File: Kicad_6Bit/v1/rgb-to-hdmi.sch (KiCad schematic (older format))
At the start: 26 parts, among them P1 CONN_02X20, P2 Conn_02x05_Odd_Even, P3 Conn_01x06, P4 CONN_01X02, SW1 SW_PUSH, SW2 SW_PUSH, SW3 SW_PUSH, SW4 SW_PUSH, U1 XC9572XL-VQFP44

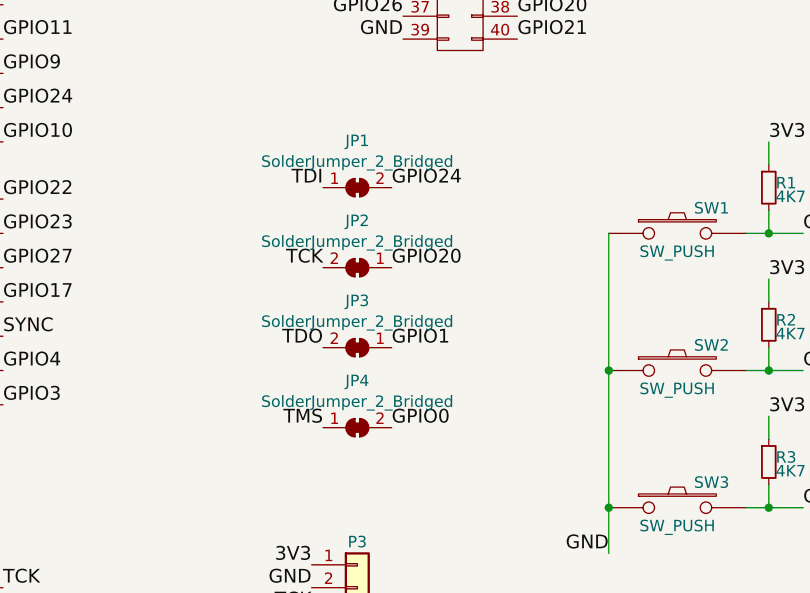
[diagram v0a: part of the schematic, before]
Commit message: Fix incorrect in system programming GPIO assignments
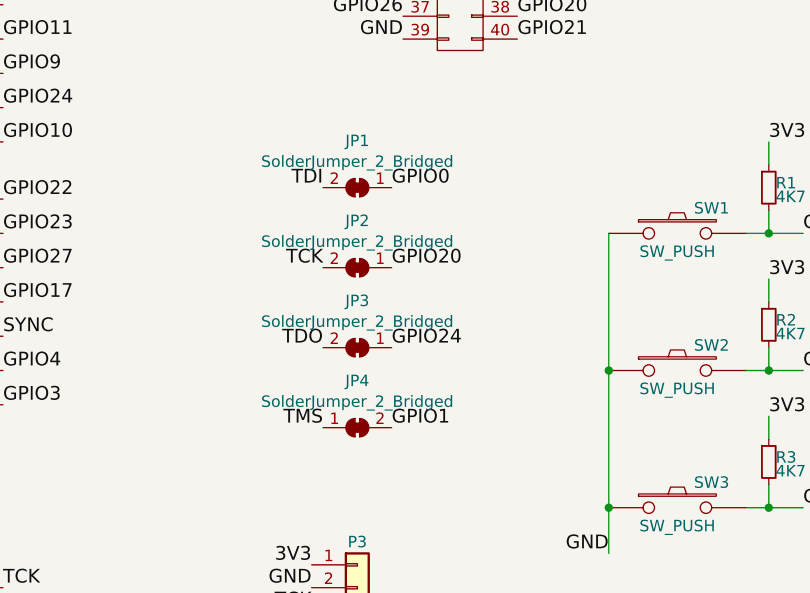
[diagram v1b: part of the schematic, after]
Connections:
- net GPIO0: now also JP1.1 (A); no longer JP4.2 (B)
- net GPIO1: now also JP4.2 (B); no longer JP3.1 (A)
- net GPIO24: now also JP3.1 (A); no longer JP1.2 (B)
- net TDI: now also JP1.2 (B); no longer JP1.1 (A)
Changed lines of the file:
@@
 TDO
 Text Label 8400 4750 0    60   ~ 0
-GPIO0
+GPIO1
 Text Label 8400 4400 0    60   ~ 0
-GPIO1
+GPIO24
 Wire Wire Line
 	9350 1150 9350 1250
@@
 F 3 "~" H 8250 3700 50  0001 C CNN
 	1    8250 3700
-	1    0    0    -1
+	-1   0    0    -1
 $EndComp
 Text Label 8400 3700 0    60   ~ 0
-GPIO24
+GPIO0
 Text Label 8100 3700 2    60   ~ 0
 TDI

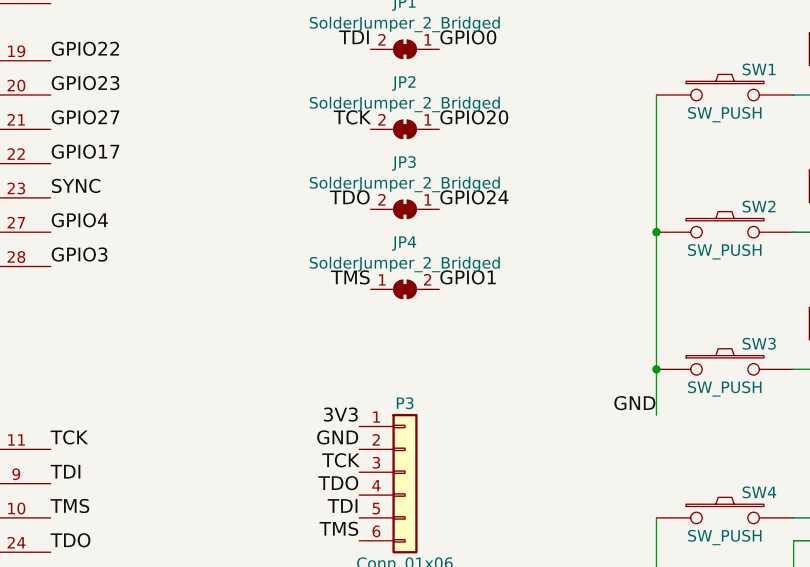
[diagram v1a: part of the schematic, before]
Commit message: Swap JP4, change P3 side & add more silk screen info
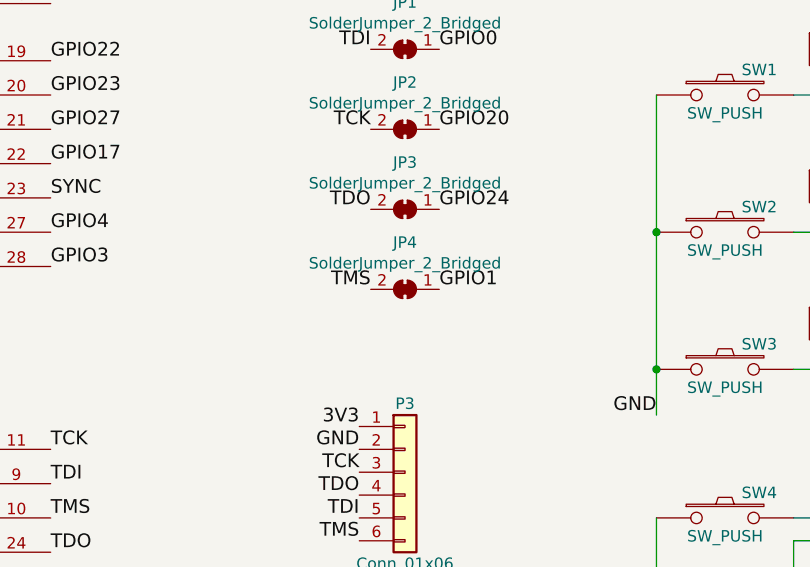
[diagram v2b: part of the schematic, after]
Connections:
- net GPIO1: now also JP4.1 (A); no longer JP4.2 (B)
- net TMS: now also JP4.2 (B); no longer JP4.1 (A)
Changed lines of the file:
@@
 F 3 "~" H 8250 4750 50  0001 C CNN
 	1    8250 4750
-	1    0    0    -1
+	-1   0    0    -1
 $EndComp
 $Comp
